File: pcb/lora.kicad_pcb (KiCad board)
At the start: 4 copper layers, 101.9 x 45.1 mm, 91 parts, among them J1 Conn_01x04, J11 Conn_Coaxial, J2 5V, J3 Conn_01x06, J4 USB_C_Receptacle_USB2.0, J5 Temp, J6 VDD, J7 UART, J8 Conn_01x04, Q1 AO3401A, Q2 AO3401A, Q3 AO3401A, Q5 AO3401A, SW1 RESET, SW2 PJ, SW3 K3-1296S-E1, U1 ME2108C50M5G, U2 ESP32-WROOM-32D, U3 2460, U4 RFM95W-868S2, U5 SCT2400, U6 CH340E

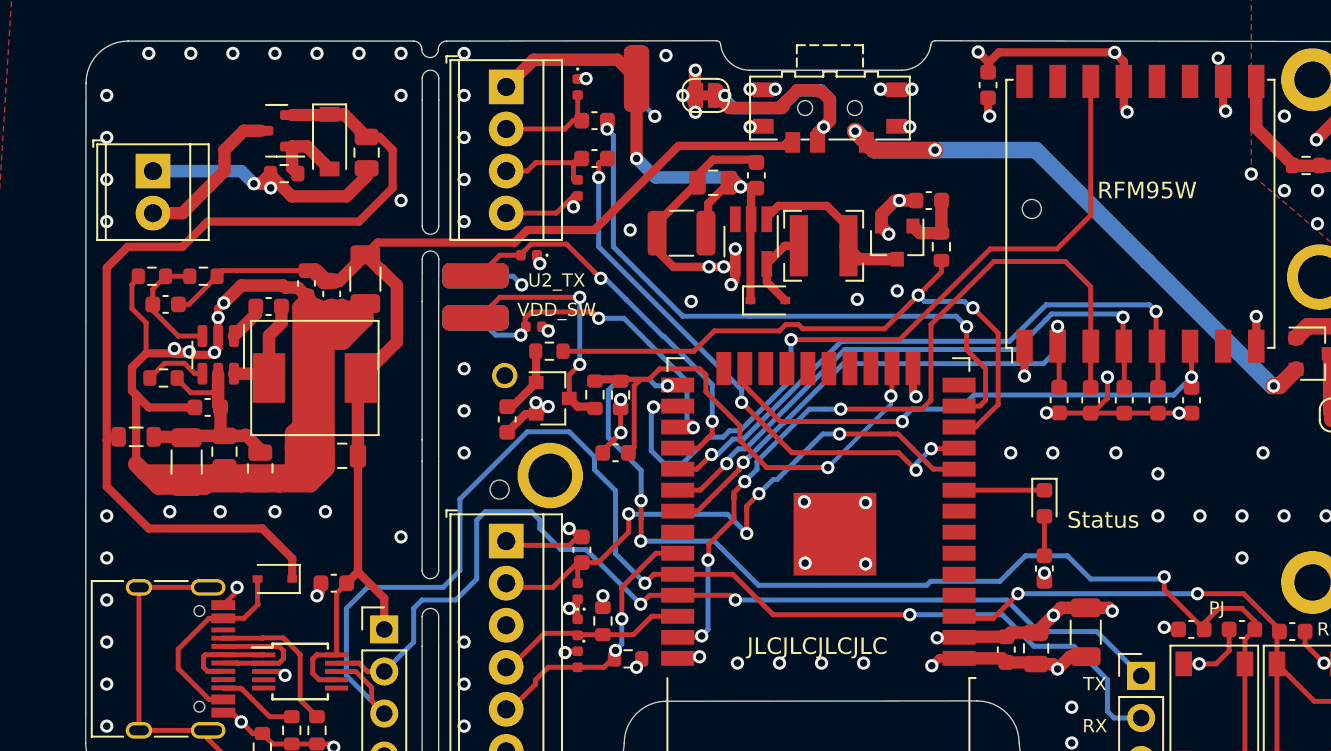
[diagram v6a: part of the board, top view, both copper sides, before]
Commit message: more silkscreen text
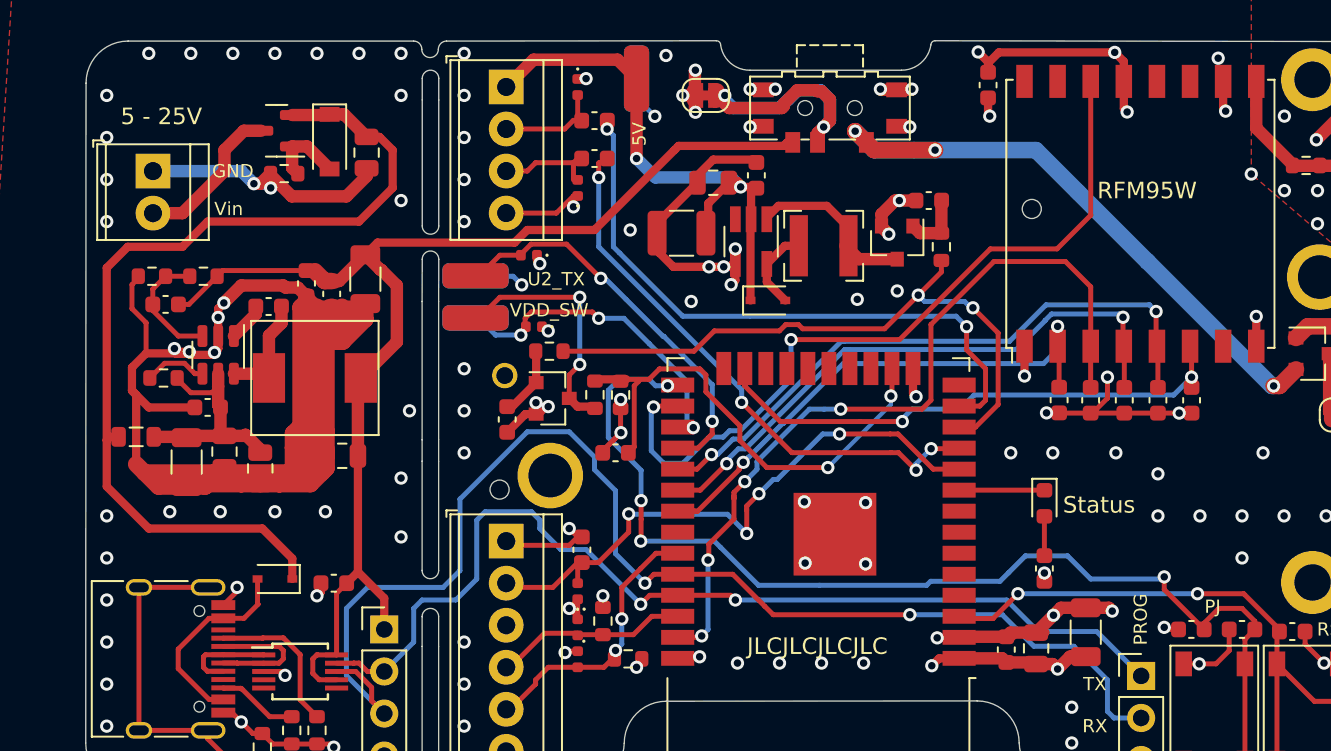
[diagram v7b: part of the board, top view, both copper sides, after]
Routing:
- net GND: vias 143 -> 145
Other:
- board text added: "3V3_EXT"
- board text added: "5 - 25V"
- board text added: "5V"
- board text added: "AI1"
- board text added: "AI2"
- board text added: "OW1"
- board text added: "PROG"
- board text added: "SCL"
- board text added: "SDA"
- board text added: "U2_RX"
- board text added: "VDD"
- board text added: "Vin"
- board text added: "v2.0 2022.01.30"
- board text removed: "v2.0 2022.01.29"
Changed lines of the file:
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@@
   (gr_line (start 168.402006 91.966713) (end 151.148051 91.966051) (layer "Edge.Cuts") (width 0.05))
   (gr_line (start 169.91 107.696) (end 169.91 116.052) (layer "Edge.Cuts") (width 0.05))
+  (gr_text "5V" (at 171.2722 94.1324) (layer "B.SilkS")
+    (effects (font (size 0.8 0.8) (thickness 0.15)) (justify mirror))
+  )
+  (gr_text "3V3_EXT" (at 162.56 127.254) (layer "B.SilkS")
+    (effects (font (size 0.8 0.8) (thickness 0.12)) (justify mirror))
+  )
+  (gr_text "AI2" (at 171.45 99.1108) (layer "B.SilkS")
+    (effects (font (size 0.8 0.8) (thickness 0.15)) (justify mirror))
+  )
   (gr_text "V_EXT/OFF" (at 190.98 99.33 90) (layer "B.SilkS")
     (effects (font (size 1 1) (thickness 0.15)) (justify mirror))
   )
+  (gr_text "AI1" (at 171.3738 96.6978) (layer "B.SilkS")
+    (effects (font (size 0.8 0.8) (thickness 0.15)) (justify mirror))
+  )
+  (gr_text "U2_RX" (at 170.6118 111.5314 90) (layer "B.SilkS")
+    (effects (font (size 0.8 0.8) (thickness 0.12)) (justify mirror))
+  )
+  (gr_text "SCL" (at 171.45 129.7686) (layer "B.SilkS")
+    (effects (font (size 0.8 0.8) (thickness 0.15)) (justify mirror))
+  )
+  (gr_text "GND" (at 150.114 99.314) (layer "B.SilkS")
+    (effects (font (size 0.8 0.8) (thickness 0.12)) (justify mirror))
+  )
+  (gr_text "VDD" (at 171.4754 122.2248) (layer "B.SilkS")
+    (effects (font (size 0.8 0.8) (thickness 0.15)) (justify mirror))
+  )
   (gr_text "pcbDesign:" (at 222.25 132.842) (layer "B.SilkS")
     (effects (font (size 1 1) (thickness 0.15)) (justify mirror))
   )
-  (gr_text "AcreLink" (at 215.646 94.742) (layer "B.SilkS")
-    (effects (font (size 1.4 1.4) (thickness 0.25)) (justify mirror))
+  (gr_text "GND" (at 170.5864 103.9876 90) (layer "B.SilkS")
+    (effects (font (size 0.8 0.8) (thickness 0.12)) (justify mirror))
+  )
+  (gr_text "SDA" (at 171.4754 132.2832) (layer "B.SilkS")
+    (effects (font (size 0.8 0.8) (thickness 0.15)) (justify mirror))
+  )
+  (gr_text "TX" (at 164.338 133.096) (layer "B.SilkS")
+    (effects (font (size 0.8 0.8) (thickness 0.12)) (justify mirror))
+  )
+  (gr_text "GND" (at 171.4754 127.127) (layer "B.SilkS")
+    (effects (font (size 0.8 0.8) (thickness 0.15)) (justify mirror))
+  )
+  (gr_text "VDD" (at 171.45 134.8486) (layer "B.SilkS")
+    (effects (font (size 0.8 0.8) (thickness 0.15)) (justify mirror))
+  )
+  (gr_text "Vin" (at 150.114 101.854) (layer "B.SilkS")
+    (effects (font (size 0.8 0.8) (thickness 0.12)) (justify mirror))
+  )
+  (gr_text "AcreLink" (at 213.868 94.488) (layer "B.SilkS")
+    (effects (font (size 2 2) (thickness 0.3)) (justify mirror))
+  )
+  (gr_text "OW1" (at 171.3484 124.7902) (layer "B.SilkS")
+    (effects (font (size 0.8 0.8) (thickness 0.15)) (justify mirror))
   )
   (gr_text "BATT" (at 196.342 97.028 90) (layer "B.SilkS")
@@
     (effects (font (size 1 1) (thickness 0.2)) (justify mirror))
   )
+  (gr_text "GND" (at 181.864 97.5614 90) (layer "B.SilkS")
+    (effects (font (size 0.8 0.8) (thickness 0.15)) (justify mirror))
+  )
   (gr_text "LifePo4 or Lithium-Thionyl-Chlorid\n3.6V MAX!" (at 200.406 123.698) (layer "B.SilkS")
     (effects (font (size 1 1) (thickness 0.15)) (justify mirror))
   )
-  (gr_text "v2.0 2022.01.29" (at 213.614 97.79) (layer "B.SilkS")
+  (gr_text "GND" (at 163.83 135.382) (layer "B.SilkS")
+    (effects (font (size 0.8 0.8) (thickness 0.12)) (justify mirror))
+  )
+  (gr_text "RX" (at 164.338 130.048) (layer "B.SilkS")
+    (effects (font (size 0.8 0.8) (thickness 0.12)) (justify mirror))
+  )
+  (gr_text "v2.0 2022.01.30" (at 213.614 97.79) (layer "B.SilkS")
     (effects (font (size 1 1) (thickness 0.15)) (justify mirror))
+  )
+  (gr_text "GND" (at 171.6532 101.854) (layer "B.SilkS")
+    (effects (font (size 0.8 0.8) (thickness 0.15)) (justify mirror))
   )
   (gr_text "JLCJLCJLCJLC" (at 192.786 128.524) (layer "F.SilkS")
@@
     (effects (font (size 0.6 0.6) (thickness 0.08)))
   )
-  (gr_text "PJ" (at 216.916 126.238) (layer "F.SilkS")
+  (gr_text "PJ" (at 216.662 126.1364) (layer "F.SilkS")
     (effects (font (size 0.8 0.8) (thickness 0.12)))
   )
@@
     (effects (font (size 0.6 0.6) (thickness 0.08)))
   )
-  (gr_text "VDD_SW" (at 177.038 108.204) (layer "F.SilkS")
+  (gr_text "VDD_SW" (at 176.5808 108.2294) (layer "F.SilkS")
     (effects (font (size 0.8 0.8) (thickness 0.12)))
   )
@@
     (effects (font (size 1 1) (thickness 0.15)))
   )
+  (gr_text "Vin" (at 157.226 102.108) (layer "F.SilkS")
+    (effects (font (size 0.8 0.8) (thickness 0.12)))
+  )
+  (gr_text "GND" (at 157.48 99.822) (layer "F.SilkS")
+    (effects (font (size 0.8 0.8) (thickness 0.12)))
+  )
   (gr_text "RX" (at 209.55 133.35) (layer "F.SilkS")
     (effects (font (size 0.8 0.8) (thickness 0.12)))
@@
     (effects (font (size 0.8 0.8) (thickness 0.12)))
   )
-  (gr_text "U2_TX" (at 177.038 106.426) (layer "F.SilkS")
+  (gr_text "U2_TX" (at 177.0126 106.3498) (layer "F.SilkS")
     (effects (font (size 0.8 0.8) (thickness 0.12)))
   )
-  (gr_text "Status" (at 210.058 120.904) (layer "F.SilkS")
+  (gr_text "Status" (at 209.804 119.9896) (layer "F.SilkS")
     (effects (font (size 1 1) (thickness 0.15)))
+  )
+  (gr_text "5V" (at 182.0418 97.5868 90) (layer "F.SilkS")
+    (effects (font (size 0.8 0.8) (thickness 0.15)))
   )
   (gr_text "TX" (at 209.55 130.81) (layer "F.SilkS")
@@
   (gr_text "here for 868 MHz\n              in free air" (at 244.18 127.64) (layer "F.SilkS")
     (effects (font (size 0.6 0.6) (thickness 0.08)))
+  )
+  (gr_text "5 - 25V" (at 153.162 96.52) (layer "F.SilkS")
+    (effects (font (size 1 1) (thickness 0.15)))
+  )
+  (gr_text "PROG" (at 212.3186 126.8984 90) (layer "F.SilkS")
+    (effects (font (size 0.8 0.8) (thickness 0.12)))
   )
   (segment (start 222.93025 97.93025) (end 224.68025 96.18025) (width 0.75) (layer "F.Cu") (net 1))
@@
   (via (at 215.852 129.588) (size 0.8) (drill 0.45) (layers "F.Cu" "B.Cu") (net 1))
   (via (at 218.44 123.19) (size 0.8) (drill 0.45) (layers "F.Cu" "B.Cu") (free) (net 1))
+  (via (at 167.64 118.364) (size 0.8) (drill 0.45) (layers "F.Cu" "B.Cu") (free) (net 1))
   (via (at 167.64 121.92) (size 0.8) (drill 0.45) (layers "F.Cu" "B.Cu") (free) (net 1))
   (via (at 207.3 129.9) (size 0.8) (drill 0.45) (layers "F.Cu" "B.Cu") (net 1))
@@
   (via (at 219.71 116.84) (size 0.8) (drill 0.45) (layers "F.Cu" "B.Cu") (free) (net 1))
   (via (at 228.6 120.65) (size 0.8) (drill 0.45) (layers "F.Cu" "B.Cu") (free) (net 1))
+  (via (at 168.148 114.3) (size 0.8) (drill 0.45) (layers "F.Cu" "B.Cu") (free) (net 1))
   (via (at 171.45 100.33) (size 0.8) (drill 0.45) (layers "F.Cu" "B.Cu") (free) (net 1))
   (via (at 193.04 129.54) (size 0.8) (drill 0.45) (layers "F.Cu" "B.Cu") (free) (net 1))
@@
     (polygon
       (pts
-        (xy 168.275 109.982)
-        (xy 168.275 119.761)
+        (xy 168.6814 110.3376)
+        (xy 166.1668 119.7864)
         (xy 162.814 119.888)
         (xy 153.34 119.75)
         (xy 150.96 120.42)
         (xy 150.749 104.394)
-        (xy 168.275 104.14)
+        (xy 168.8084 104.2162)
       )
     )
